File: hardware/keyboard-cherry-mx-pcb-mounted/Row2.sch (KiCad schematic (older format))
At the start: 30 parts, among them SW74 Tab, SW75 i, SW76 q, SW77 o, SW78 w, SW79 p, SW80 e, SW81 [, SW82 r, SW83 ], SW84 t, SW85 \\, SW86 y, SW87 PgUp, SW88 u

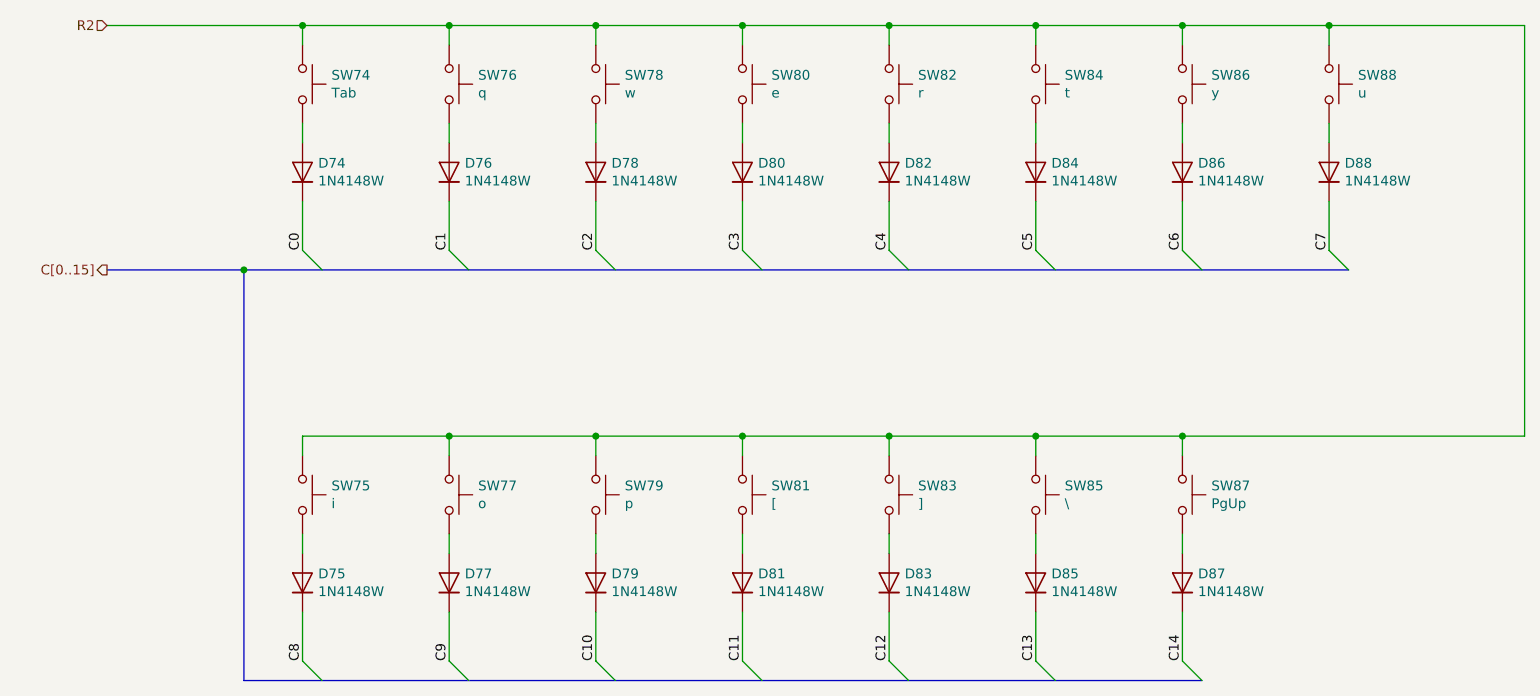
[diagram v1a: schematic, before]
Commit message: Adds completed sensor and power connections. Still need to add USB footprint then sch are done for version 1.0
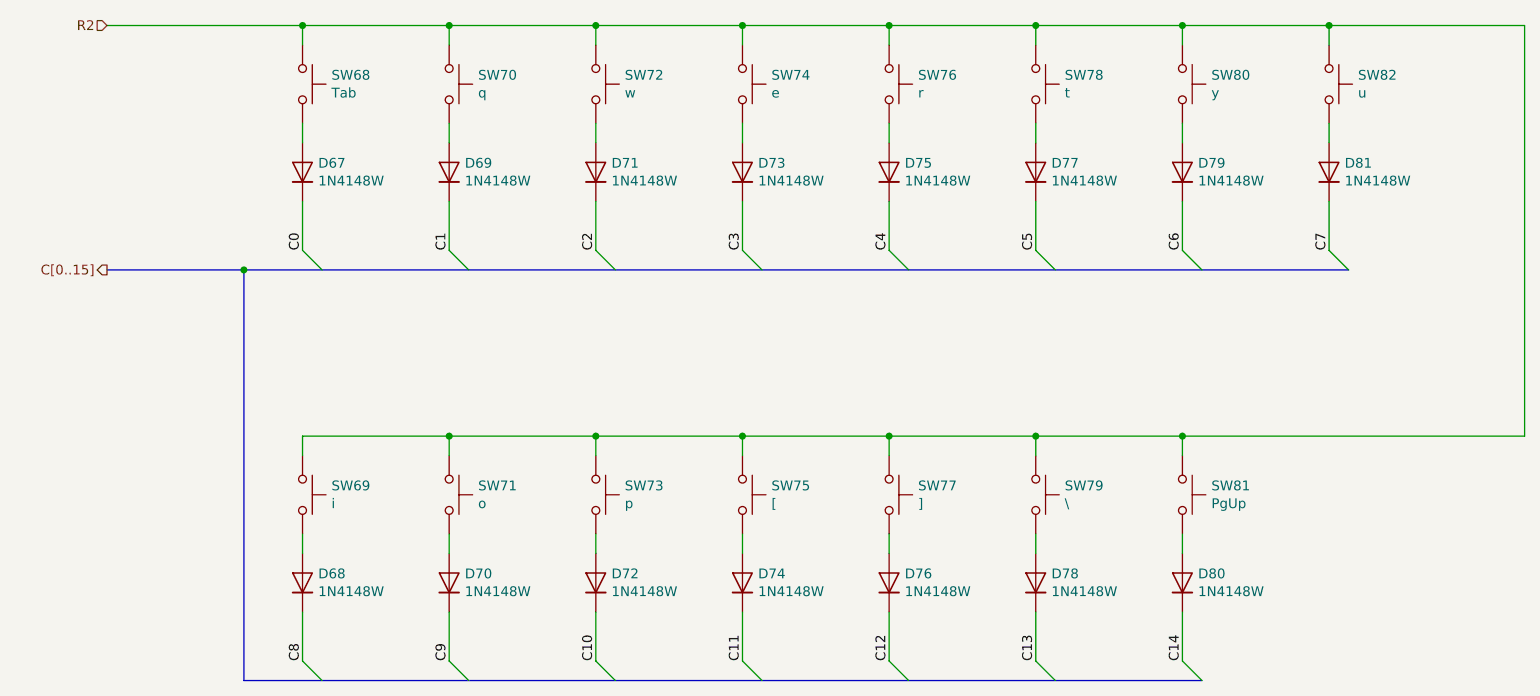
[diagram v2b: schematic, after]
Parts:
- renumbered D74 to D67, D75 to D68, D76 to D69, D77 to D70, D78 to D71, D79 to D72, D80 to D73, D81 to D74, D82 to D75, D83 to D76, D84 to D77, D85 to D78, D86 to D79, D87 to D80, D88 to D81, SW74 to SW68, SW75 to SW69, SW76 to SW70, SW77 to SW71, SW78 to SW72, SW79 to SW73, SW80 to SW74, SW81 to SW75, SW82 to SW76, SW83 to SW77, SW84 to SW78, SW85 to SW79, SW86 to SW80, SW87 to SW81, SW88 to SW82

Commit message: Aligns the keys so the column connections are more consistent. e.g. right most keys will have same column connection.
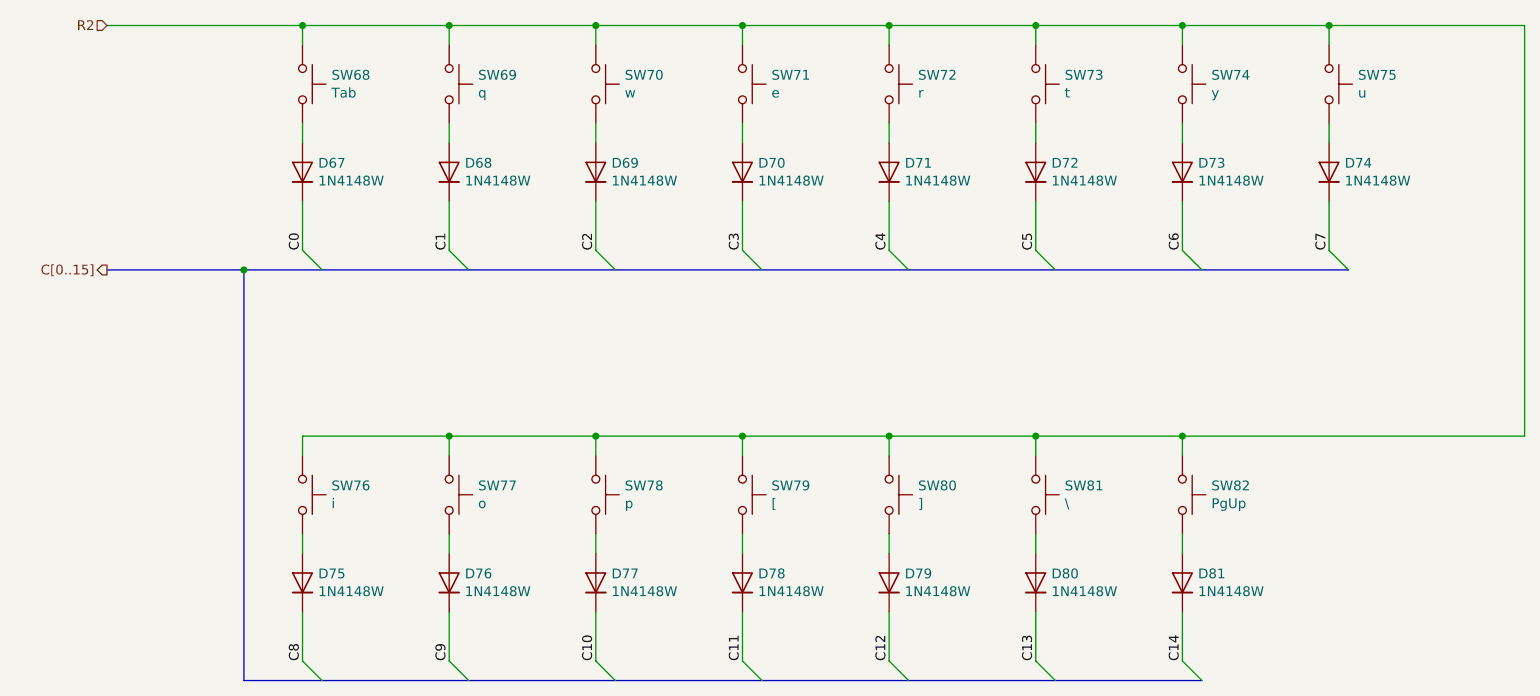
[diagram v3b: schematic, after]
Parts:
- renumbered D69 to D68, D71 to D69, D73 to D70, D75 to D71, D77 to D72, D79 to D73, D81 to D74, D68 to D75, D70 to D76, D72 to D77, D74 to D78, D76 to D79, D78 to D80, D80 to D81, SW70 to SW69, SW72 to SW70, SW74 to SW71, SW76 to SW72, SW78 to SW73, SW80 to SW74, SW82 to SW75, SW69 to SW76, SW71 to SW77, SW73 to SW78, SW75 to SW79, SW77 to SW80, SW79 to SW81, SW81 to SW82

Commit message: Adds labels for each key and creates gerber files.
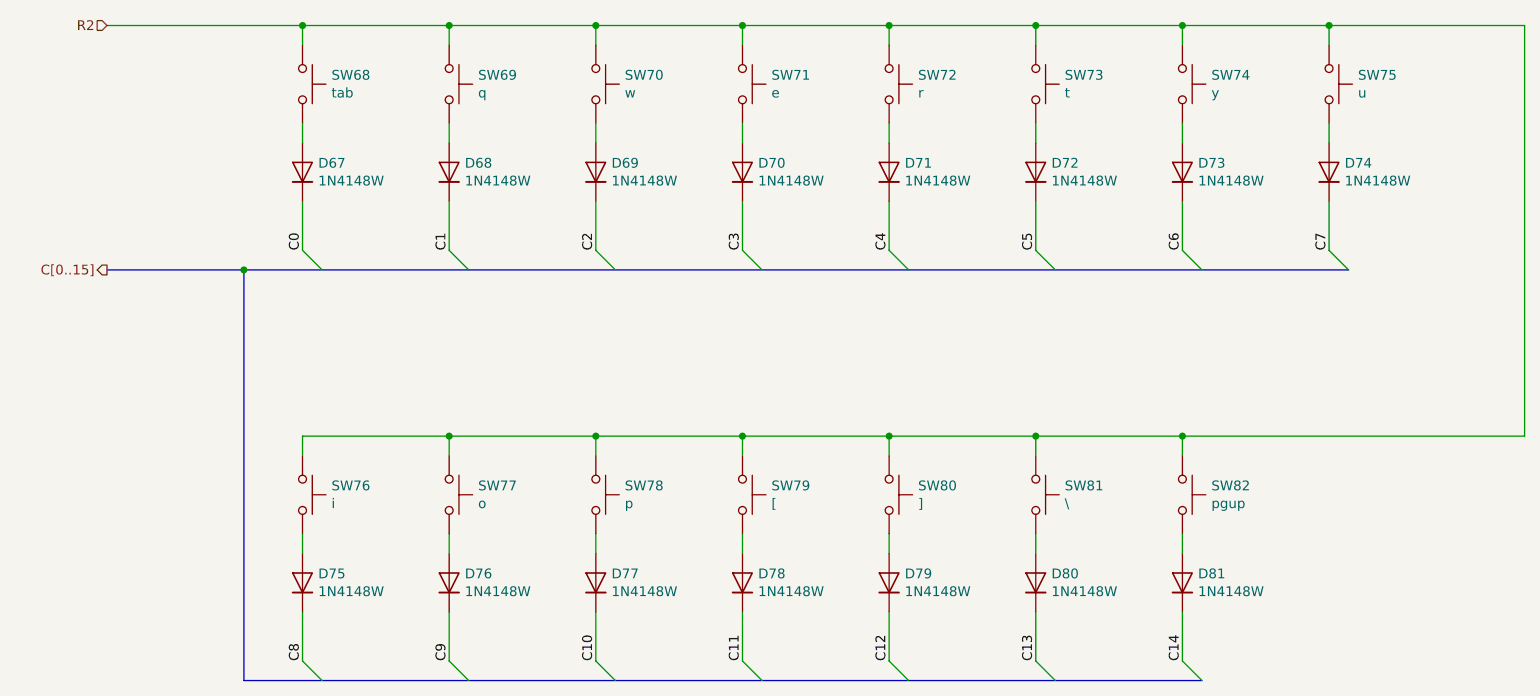
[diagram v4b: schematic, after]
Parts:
- SW68: value Tab -> tab
- SW82: value PgUp -> pgup
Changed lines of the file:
@@
 AR Path="/5E697948/5E785F4F/5E818F0E" Ref="SW?"  Part="1"
 F 0 "SW68" V 3104 2548 50  0000 L CNN
-F 1 "Tab" V 3195 2548 50  0000 L CNN
+F 1 "tab" V 3195 2548 50  0000 L CNN
 F 2 "Button_Switch_Keyboard:SW_Cherry_MX_1.50u_PCB" H 3150 2600 50  0001 C CNN
 F 3 "~" H 3150 2600 50  0001 C CNN
@@
 AR Path="/5E697948/5E785F4F/5E818F2A" Ref="SW?"  Part="1"
 F 0 "SW82" V 7604 4648 50  0000 L CNN
-F 1 "PgUp" V 7695 4648 50  0000 L CNN
+F 1 "pgup" V 7695 4648 50  0000 L CNN
 F 2 "Button_Switch_Keyboard:SW_Cherry_MX_1.00u_PCB" H 7650 4700 50  0001 C CNN
 F 3 "~" H 7650 4700 50  0001 C CNN
